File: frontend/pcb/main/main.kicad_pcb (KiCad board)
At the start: 2 copper layers, 51 x 49 mm, 35 parts, among them J1 Ext, J2 Conn_01x03, J3 Conn_01x09, J4 Debug, J5 RS485, J6 Conn_01x04, J7 Conn_01x02, Q1 MMBT3904, Q2 MMBT3904, U1 ESP32-WROOM-32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

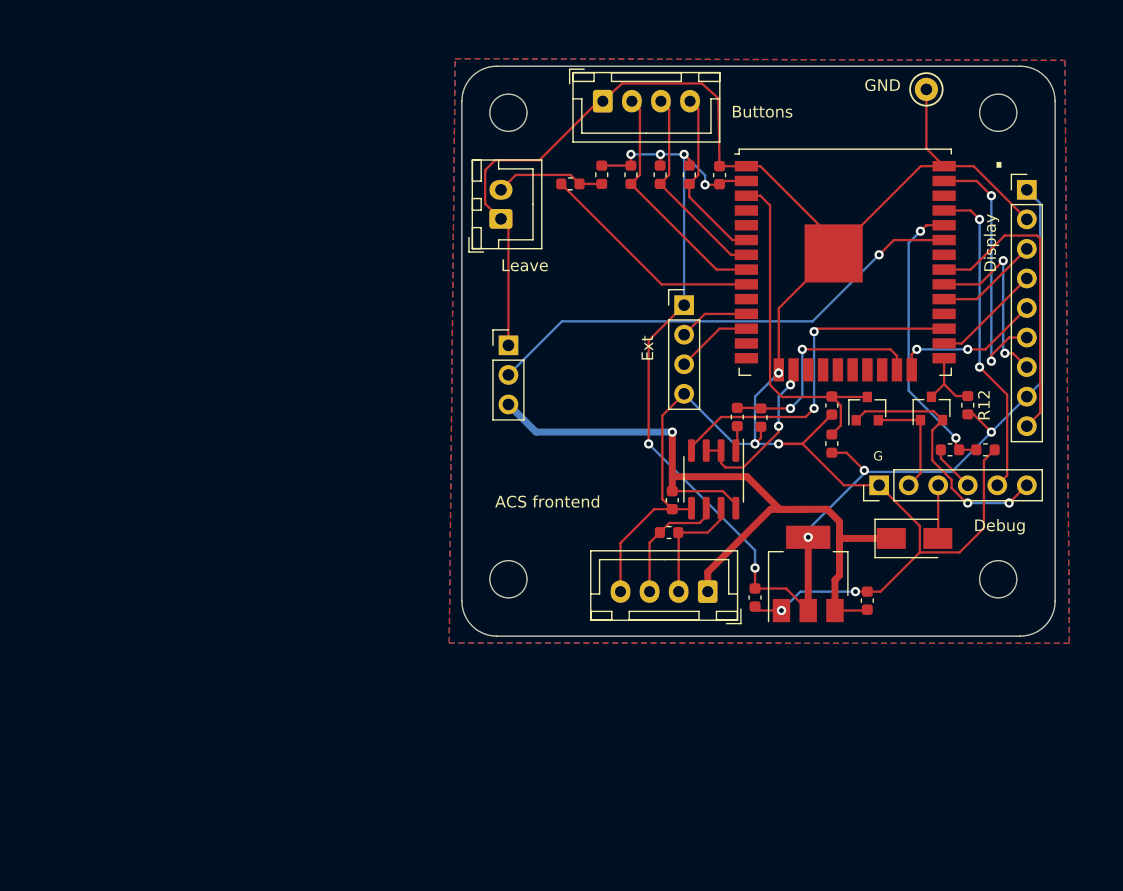
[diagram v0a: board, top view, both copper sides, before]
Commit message: Start placing additional components.
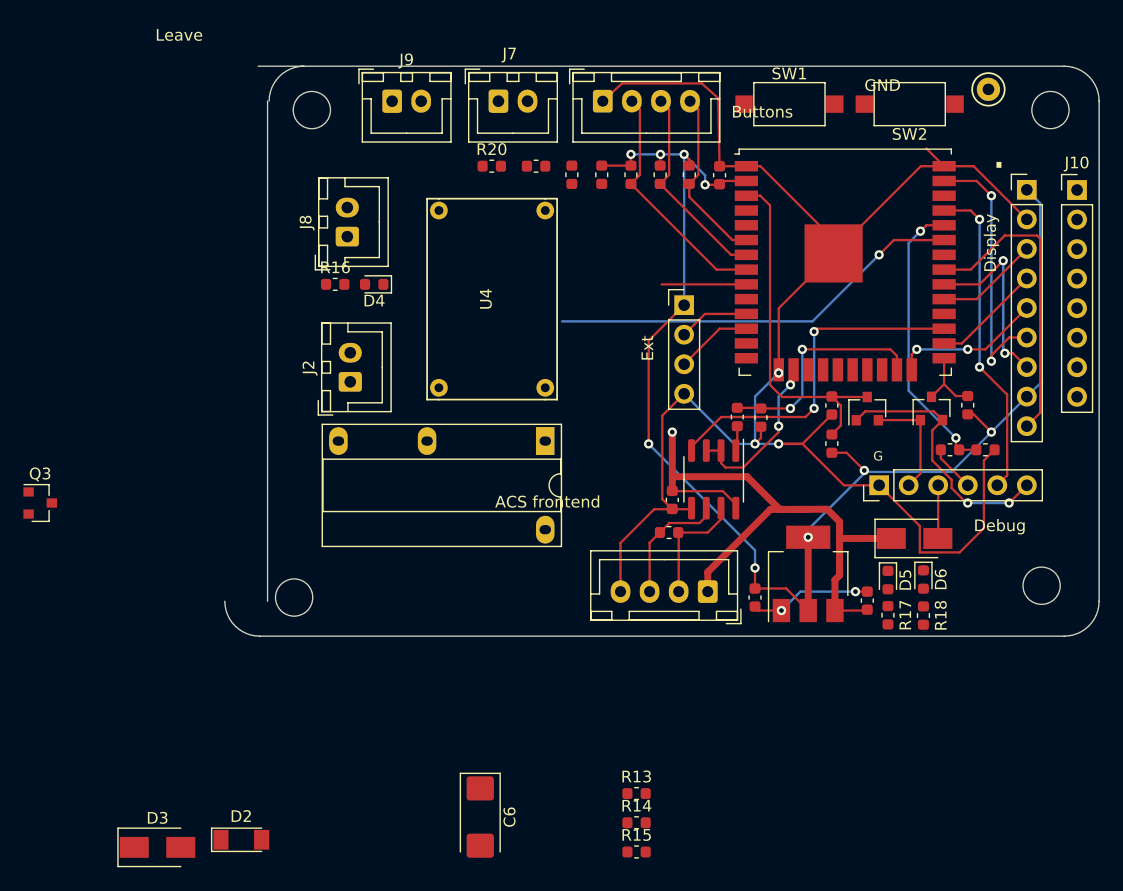
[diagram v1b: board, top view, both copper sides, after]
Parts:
- added C3: 100n, Capacitor_SMD:C_0603_1608Metric, F.Cu at (69.1, 98.3)
- added D2: 1N4148, Diode_SMD:D_MiniMELF, F.Cu at (32.0, 127.5)
- added D3: MBRA210LT3, Diode_SMD:D_SMA, F.Cu at (24.8, 128.2)
- added D4: LED, LED_SMD:LED_0603_1608Metric, F.Cu at (43.5, 79.8)
- added D5: LED, LED_SMD:LED_0603_1608Metric, F.Cu at (87.6, 105.2)
- added D6: LED, LED_SMD:LED_0603_1608Metric, F.Cu at (90.7, 105.1)
- added J10: Display1443, Connector_PinHeader_2.54mm:PinHeader_1x08_P2.54mm_Vertical, F.Cu at (103.9, 71.6)
- added J8: Conn_01x02, Connector_JST:JST_XH_B2B-XH-A_1x02_P2.50mm_Vertical, F.Cu at (41.1, 75.7)
- added J9: Conn_01x02, Connector_JST:JST_XH_B2B-XH-A_1x02_P2.50mm_Vertical, F.Cu at (45.0, 64.0)
- added K1: G6B-1114C-US5DC, modules:DIL-relay, F.Cu at (58.2, 93.2)
- added Q3: BSS138, Package_TO_SOT_SMD:SOT-23, F.Cu at (14.7, 98.6)
- added R13: 10K, Resistor_SMD:R_0603_1608Metric, F.Cu at (66.0, 123.5)
- added R14: 1K, Resistor_SMD:R_0603_1608Metric, F.Cu at (66.0, 126.0)
- added R15: 4R7, Resistor_SMD:R_0603_1608Metric, F.Cu at (66.0, 128.6)
- added R16: 10k, Resistor_SMD:R_0603_1608Metric, F.Cu at (40.1, 79.8)
- added R17: 2k7, Resistor_SMD:R_0603_1608Metric, F.Cu at (87.6, 108.2)
- added R18: 1k2, Resistor_SMD:R_0603_1608Metric, F.Cu at (90.7, 108.2)
- added R19: 1k, Resistor_SMD:R_0603_1608Metric, F.Cu at (60.5, 70.3)
- added R20: 10k, Resistor_SMD:R_0603_1608Metric, F.Cu at (53.6, 69.6)
- added SW1: SW_SPST, Button_Switch_SMD:SW_SPST_CK_RS282G05A3, F.Cu at (79.2, 64.3)
- added SW2: SW_SPST, Button_Switch_SMD:SW_SPST_CK_RS282G05A3, F.Cu at (89.5, 64.3)
- added U4: DSN-MINI-360, modules:DSN-MINI-360, F.Cu at (53.6, 81.0)
- C6: value 100n -> 220u; footprint Capacitor_SMD:C_0603_1608Metric -> Capacitor_Tantalum_SMD:CP_EIA-6032-28_Kemet-C
- J2: value Conn_01x03 -> CONN_01X02; footprint Connector_PinHeader_2.54mm:PinHeader_1x03_P2.54mm_Vertical -> Connector_JST:JST_XH_B2B-XH-A_1x02_P2.50mm_Vertical
- J3: value Conn_01x09 -> Display4020
- moved C6 31.9 mm to (52.6, 125.6)
- moved H2 18.5 mm to (36.6, 106.7)
- moved H1 16.9 mm to (38.1, 64.8)
- moved J2 14.0 mm to (41.4, 88.1), turned to 90 degrees
- moved J7 10.1 mm to (54.1, 64.0), turned to 0 degrees
- moved TP1 5.33 mm to (96.3, 63.0)
- moved H3 4.50 mm to (101.6, 64.8)
- moved H4 3.77 mm to (100.8, 105.7)
- moved R10 3.32 mm to (57.4, 69.6)
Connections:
- net /MCU_RX0 renamed MCU_RX0
- net /MCU_TX0 renamed MCU_TX0
- net Display_DC renamed Display_A0/DC
- net Display_SDI renamed Display_SDA/SDI
- C6 pad 1: +5V -> Net-(D2-K)
- J2 pad 2: Relay -> Net-(J2-Pin_2)
- U1 pad 36: unconnected-(U1-IO22-Pad36) -> Door
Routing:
- net GND: track 194.1 -> 154.9 mm
- net +5V: track 69.3 -> 54.2 mm
- net B4: track 19.5 -> 7.28 mm
- net Net-(J7-Pin_2): track 9.52 -> 0.00 mm
- net Relay: track 42.3 -> 35.7 mm
- removed copper zone on B.Cu, net GND
- removed copper zone on F.Cu, net GND
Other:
- board size 51 x 49 mm -> 75.2 x 49 mm

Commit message: Place remaining components.
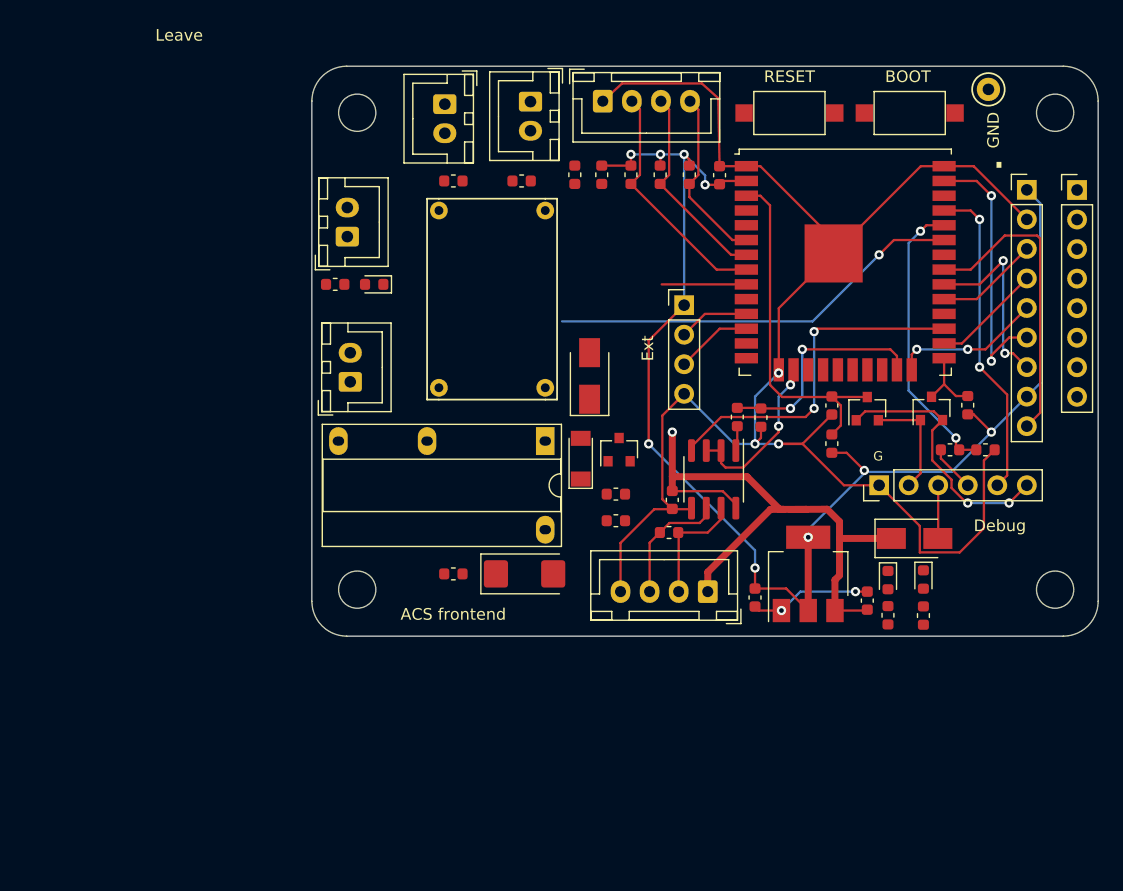
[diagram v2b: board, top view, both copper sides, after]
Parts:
- moved D3 55.0 mm to (62.0, 87.6), turned to 90 degrees
- moved Q3 50.0 mm to (64.5, 94.0), turned to 90 degrees
- moved D2 43.9 mm to (61.2, 94.7), turned to 90 degrees
- moved R15 28.6 mm to (50.3, 104.6), turned to 180 degrees
- moved R14 26.0 mm to (64.2, 100.1)
- moved R13 25.8 mm to (64.2, 97.8)
- moved C6 21.2 mm to (56.4, 104.6), turned to 0 degrees
- moved H2 5.47 mm to (42.0, 106.0)
- moved J9 4.54 mm to (49.5, 64.3), turned to -90 degrees
- moved H1 3.91 mm to (42.0, 65.0)
- moved R20 3.54 mm to (50.3, 70.9)
- moved J7 2.75 mm to (56.9, 64.0), turned to -90 degrees
- moved R10 1.78 mm to (56.1, 70.9)
- moved H4 1.21 mm to (102.0, 106.0)
- moved SW1 0.76 mm to (79.2, 65.0)
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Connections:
- J2 pad 1: GND -> Net-(J2-Pin_1)
- J2 pad 2: Net-(J2-Pin_2) -> GND
- K1 pad 3: +12V -> Net-(J2-Pin_1)
- K1 pad 4: Net-(J2-Pin_2) -> +12V
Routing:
- net GND: track 154.9 -> 152.7 mm
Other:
- board size 75.2 x 49 mm -> 67.6 x 49 mm
- board text added: "BOOT"
- board text added: "RESET"
- board text removed: "Buttons"
- board text removed: "Display"

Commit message: Complete routing.
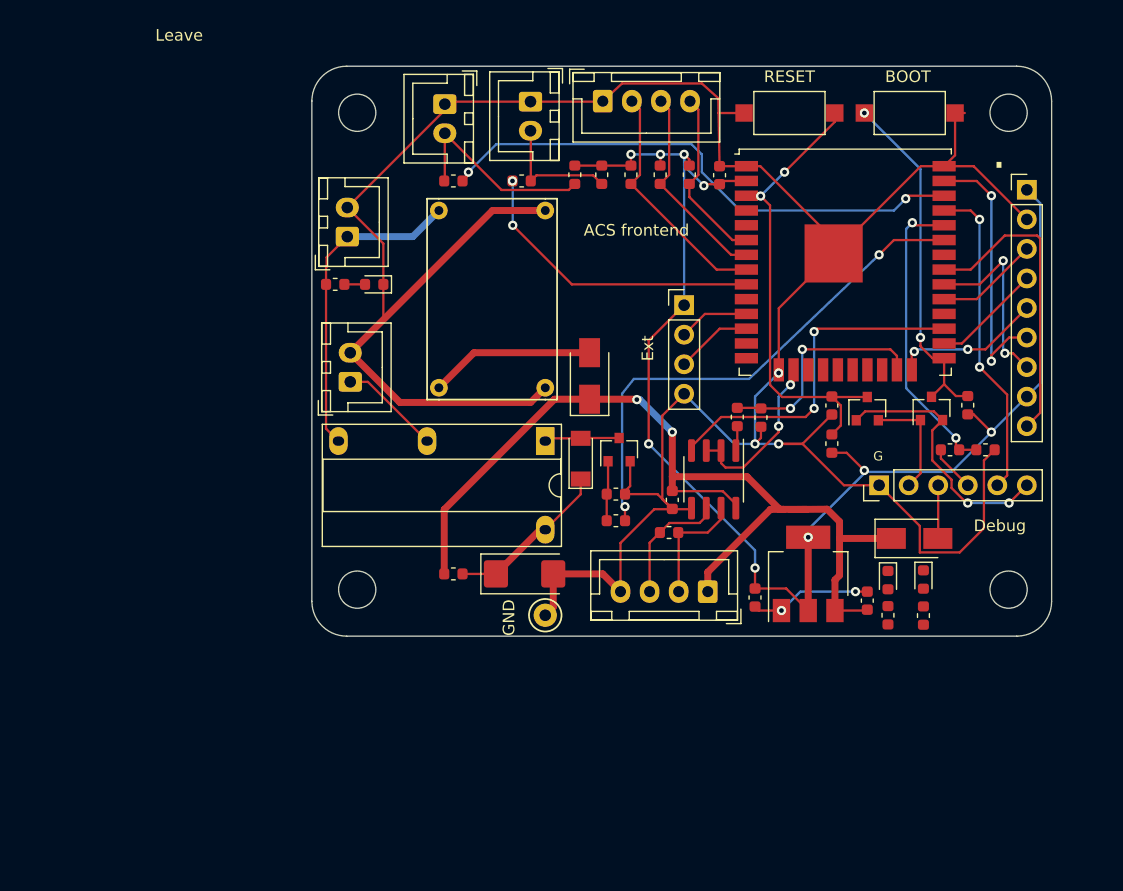
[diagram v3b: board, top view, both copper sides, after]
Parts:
- removed J10: Display1443, Connector_PinHeader_2.54mm:PinHeader_1x08_P2.54mm_Vertical
- moved TP1 59.1 mm to (58.2, 108.2)
- moved H3 4.00 mm to (98.0, 65.0)
- moved H4 4.00 mm to (98.0, 106.0)
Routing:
- net GND: track 152.7 -> 260.5 mm
- net Door: track 0.00 -> 46.6 mm, vias 0 -> 2
- net +5V: track 54.2 -> 84.5 mm, vias 1 -> 2
- net +12V: track 0.00 -> 27.6 mm
- net BOOT: track 6.22 -> 30.7 mm, vias 0 -> 2
- net B4: track 7.28 -> 26.0 mm, vias 0 -> 2
- net Net-(J9-Pin_2): track 0.00 -> 17.5 mm
- net Net-(D2-K): track 0.00 -> 14.3 mm
- net Net-(D3-A): track 0.00 -> 14.2 mm
- net Net-(J7-Pin_2): track 0.00 -> 10.9 mm
- net RESET: track 30.5 -> 40.3 mm, vias 0 -> 2
- net Net-(J2-Pin_1): track 0.00 -> 8.71 mm
- net Relay: track 35.7 -> 44.1 mm, vias 1 -> 2
- net Net-(D2-A): track 0.00 -> 6.46 mm
- net Net-(Q3-G): track 0.00 -> 5.16 mm
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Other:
- board size 67.6 x 49 mm -> 63.6 x 49 mm

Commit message: Fix last cosmetic issues.
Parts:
- moved D6 0.05 mm to (90.7, 105.2)
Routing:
- net +3V3: track 122.8 -> 133.2 mm, vias 9 -> 11
- net GND: track 260.5 -> 268.5 mm
- net +5V: track 84.5 -> 86.8 mm
- net Net-(D6-A): track 0.00 -> 1.47 mm
- net Net-(D5-A): track 0.00 -> 1.45 mm
- added copper zone on B.Cu, net GND
- added copper zone on F.Cu, net GND
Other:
- board text added: "12V IN"
- board text added: "485"
- board text added: "DOOR"
- board text added: "LOCK"
- board text added: "LV"

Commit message: Update
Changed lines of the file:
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@@
       (sketchpadsonfab false)
       (subtractmaskfromsilk false)
-      (outputformat 5)
+      (outputformat 1)
       (mirror false)
       (drillshape 0)
       (scaleselection 1)
-      (outputdirectory "")
+      (outputdirectory "gerber/")
     )
   )
@@
       (effects (font (size 1 1) (thickness 0.15)))
     )
-    (pad "1" smd roundrect (at -2.4625 0) (size 2.075 2.35) (layers "F.Cu" "F.Paste" "F.Mask") (roundrect_rratio 0.120482)
+    (pad "1" smd roundrect (at -2.4625 0) (size 2.075 2.35) (layers "F.Cu" "F.Paste" "F.Mask") (roundrect_rratio 0.1204819277)
       (net 12 "Net-(D2-K)") (pintype "passive")
     )
-    (pad "2" smd roundrect (at 2.4625 0) (size 2.075 2.35) (layers "F.Cu" "F.Paste" "F.Mask") (roundrect_rratio 0.120482)
+    (pad "2" smd roundrect (at 2.4625 0) (size 2.075 2.35) (layers "F.Cu" "F.Paste" "F.Mask") (roundrect_rratio 0.1204819277)
       (net 2 "GND") (pintype "passive")
     )
@@
       (effects (font (size 1 1) (thickness 0.15)))
     )
-    (pad "1" thru_hole roundrect (at 0 0 90) (size 1.7 2) (drill 1) (layers "*.Cu" "*.Mask") (roundrect_rratio 0.147059)
+    (pad "1" thru_hole roundrect (at 0 0 90) (size 1.7 2) (drill 1) (layers "*.Cu" "*.Mask") (roundrect_rratio 0.1470588235)
       (net 51 "+12V") (pinfunction "Pin_1") (pintype "passive")
     )
@@
       (effects (font (size 1 1) (thickness 0.15)))
     )
-    (pad "1" thru_hole roundrect (at 0 0 270) (size 1.7 2) (drill 1) (layers "*.Cu" "*.Mask") (roundrect_rratio 0.147059)
+    (pad "1" thru_hole roundrect (at 0 0 270) (size 1.7 2) (drill 1) (layers "*.Cu" "*.Mask") (roundrect_rratio 0.1470588235)
       (net 2 "GND") (pinfunction "Pin_1") (pintype "passive")
     )
@@
       (effects (font (size 1 1) (thickness 0.15)))
     )
-    (pad "1" thru_hole roundrect (at 0 0 90) (size 1.7 2) (drill 1) (layers "*.Cu" "*.Mask") (roundrect_rratio 0.147059)
+    (pad "1" thru_hole roundrect (at 0 0 90) (size 1.7 2) (drill 1) (layers "*.Cu" "*.Mask") (roundrect_rratio 0.1470588235)
       (net 47 "Net-(J2-Pin_1)") (pinfunction "Pin_1") (pintype "passive")
     )

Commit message: Remove orphan silk screen.
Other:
- board text removed: "Leave"
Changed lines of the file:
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@@
-(kicad_pcb (version 20230606) (generator pcbnew)
+(kicad_pcb (version 20231007) (generator pcbnew)
   (general
     (thickness 1.6)
@@
     (effects (font (size 1 1) (thickness 0.15)) (justify left bottom))
   )
-  (gr_text "Leave" (at 24.638 58.928 0) (layer "F.SilkS")
-    (effects (font (size 1 1) (thickness 0.15)) (justify left bottom))
-  )
